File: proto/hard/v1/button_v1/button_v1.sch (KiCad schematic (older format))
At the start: 75 parts, among them J1 Conn_01x06_Female, J10 Conn_01x01_Female, J11 Conn_01x01_Female, J12 Conn_01x01_Female, J13 Conn_01x01_Female, J14 K3-2336D-combi, J15 Conn_01x03_Male, J16 Conn_01x01_Male, J2 Conn_01x06_Female, J3 Conn_01x06_Female, J4 Conn_01x06_Female, J7 Conn_01x04_Female, J9 Conn_01x01_Female, Q1 TP0610T, Q3 TP0610T, Q6 UMG8N, Q7 UMG8N, U1 LCD_2.8_SPI, U11 TC305, U12 OLED_0.96_I2C, U13 74HC595, U2 STM32F103C8Tx, U6 LM339, Y1 8MHz

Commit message: Schematic libs clean-up
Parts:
- U12: footprint MyModules:OLED_0.96_I2C -> brbuttonsystem:OLED_0.96_I2C; symbol MyModules:OLED_0.96_I2C -> brbuttonsystem:OLED_0.96_I2C
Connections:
- wire segments 191 -> 190
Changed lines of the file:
@@
 $Comp
 L brbuttonsystem:K3-2336D-combi J14
-U 1 1 5D188189
+U 2 1 5D188189
 P 7850 2850
 F 0 "J14" H 7950 2900 50  0000 C CNN
@@
 F 2 "brbuttonsystem:K3-2346D" H 7850 2850 50  0001 C CNN
 F 3 "" H 7850 2850 50  0001 C CNN
-	1    7850 2850
+	2    7850 2850
 	1    0    0    -1
 $EndComp
@@
 $EndComp
 Wire Wire Line
-	10250 1450 10250 1550
-Connection ~ 10250 1450
-Wire Wire Line
 	10250 1550 10100 1550
-Wire Wire Line
-	10250 1350 10250 1450
 Wire Wire Line
 	10100 1250 10250 1250
@@
 DISP_SCL
 $Comp
-L MyModules:OLED_0.96_I2C U12
+L brbuttonsystem:OLED_0.96_I2C U12
 U 1 1 5D23818B
 P 10350 950
 F 0 "U12" H 10350 1000 50  0000 L CNN
 F 1 "OLED_0.96_I2C" H 10350 300 50  0000 L CNN
-F 2 "MyModules:OLED_0.96_I2C" H 10350 950 50  0001 C CNN
+F 2 "brbuttonsystem:OLED_0.96_I2C" H 10350 950 50  0001 C CNN
 F 3 "" H 10350 950 50  0001 C CNN
 	1    10350 950
@@
 	-1   0    0    -1
 $EndComp
+Wire Wire Line
+	10250 1350 10250 1550
 $EndSCHEMATC

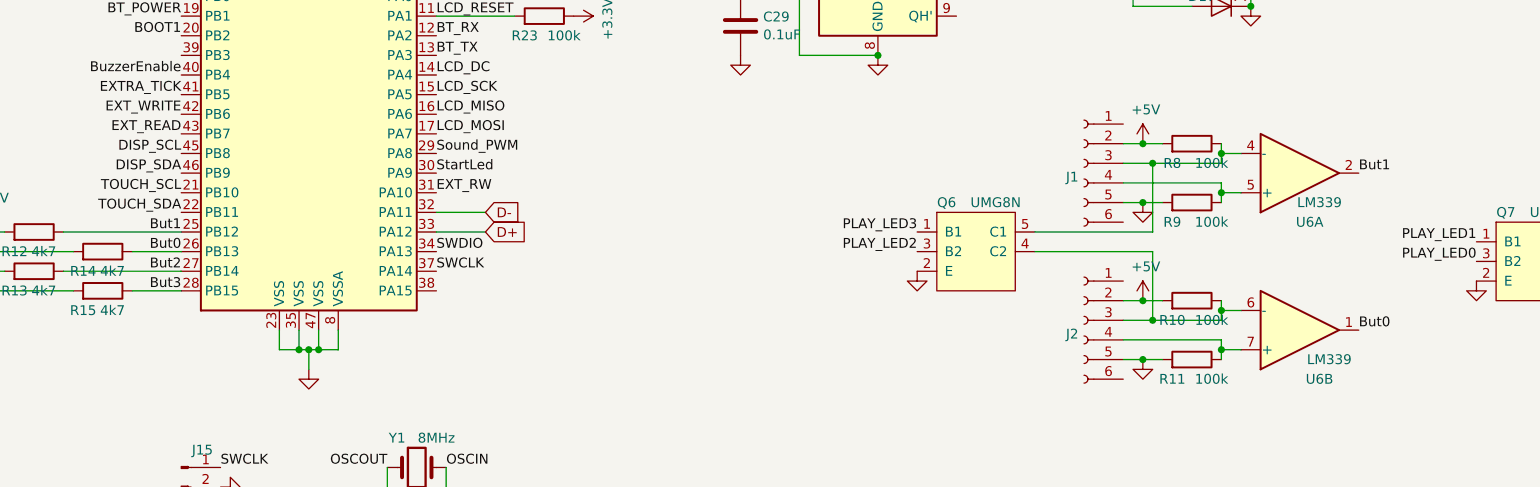
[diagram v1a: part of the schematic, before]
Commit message: Added example project with button connection schematic only. Corrected "dip" pins assignment to comply with main project.
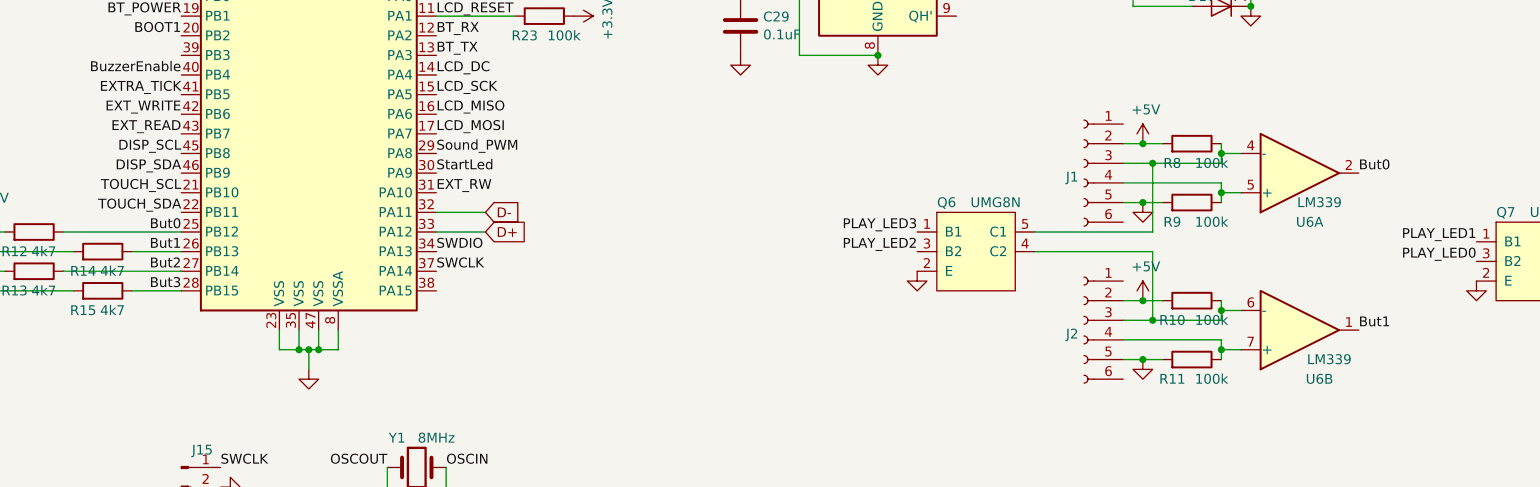
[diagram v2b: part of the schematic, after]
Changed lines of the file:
@@
 EESchema Schematic File Version 4
-LIBS:button_v1-cache
 EELAYER 29 0
 EELAYER END
@@
 $EndComp
 Connection ~ 10950 3900
+Text Label 7850 5000 0    50   ~ 0
+But0
 Text Label 7850 5800 0    50   ~ 0
-But0
-Text Label 7850 5000 0    50   ~ 0
 But1
 Text Label 10800 5000 0    50   ~ 0
@@
 Text Label 1850 5500 2    50   ~ 0
 But2
+Text Label 1850 5400 2    50   ~ 0
+But1
 Text Label 1850 5300 2    50   ~ 0
-But1
-Text Label 1850 5400 2    50   ~ 0
 But0
 Wire Wire Line

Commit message: Started schematic and PCB rework. Generated button_v1.pdf was left out of sync intentionally.
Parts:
- removed C28: 0.1uF, Capacitor_SMD:C_0805_2012Metric_Pad1.15x1.40mm_HandSolder, symbol Device:C
- removed D14, D15, D16, D17: LED, LED_THT:LED_D3.0mm_Clear, symbol Device:LED
- removed J14: K3-2336D-combi, brbuttonsystem:K3-2346D, symbol brbuttonsystem:K3-2336D-combi
- removed R12, R13, R14, R15, R41, R42: 4k7, Resistor_SMD:R_0805_2012Metric_Pad1.15x1.40mm_HandSolder, symbol Device:R
- removed U12: OLED_0.96_I2C, brbuttonsystem:OLED_0.96_I2C, symbol brbuttonsystem:OLED_0.96_I2C
- added J14: K3-2235D, brbuttonsystem:K3-2235D, symbol brbuttonsystem:K3-2235D
- added RN1: 4k7, Resistor_THT:R_Array_SIP5, symbol Device:R_Network04
- J7: footprint Connector_PinHeader_2.54mm:PinHeader_1x04_P2.54mm_Vertical -> Connector_PinHeader_2.54mm:PinHeader_1x04_P2.54mm_Horizontal
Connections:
- wire segments 190 -> 163
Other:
- moved on the sheet: D10, D11, D12, D13, R43, R44, R45, R46

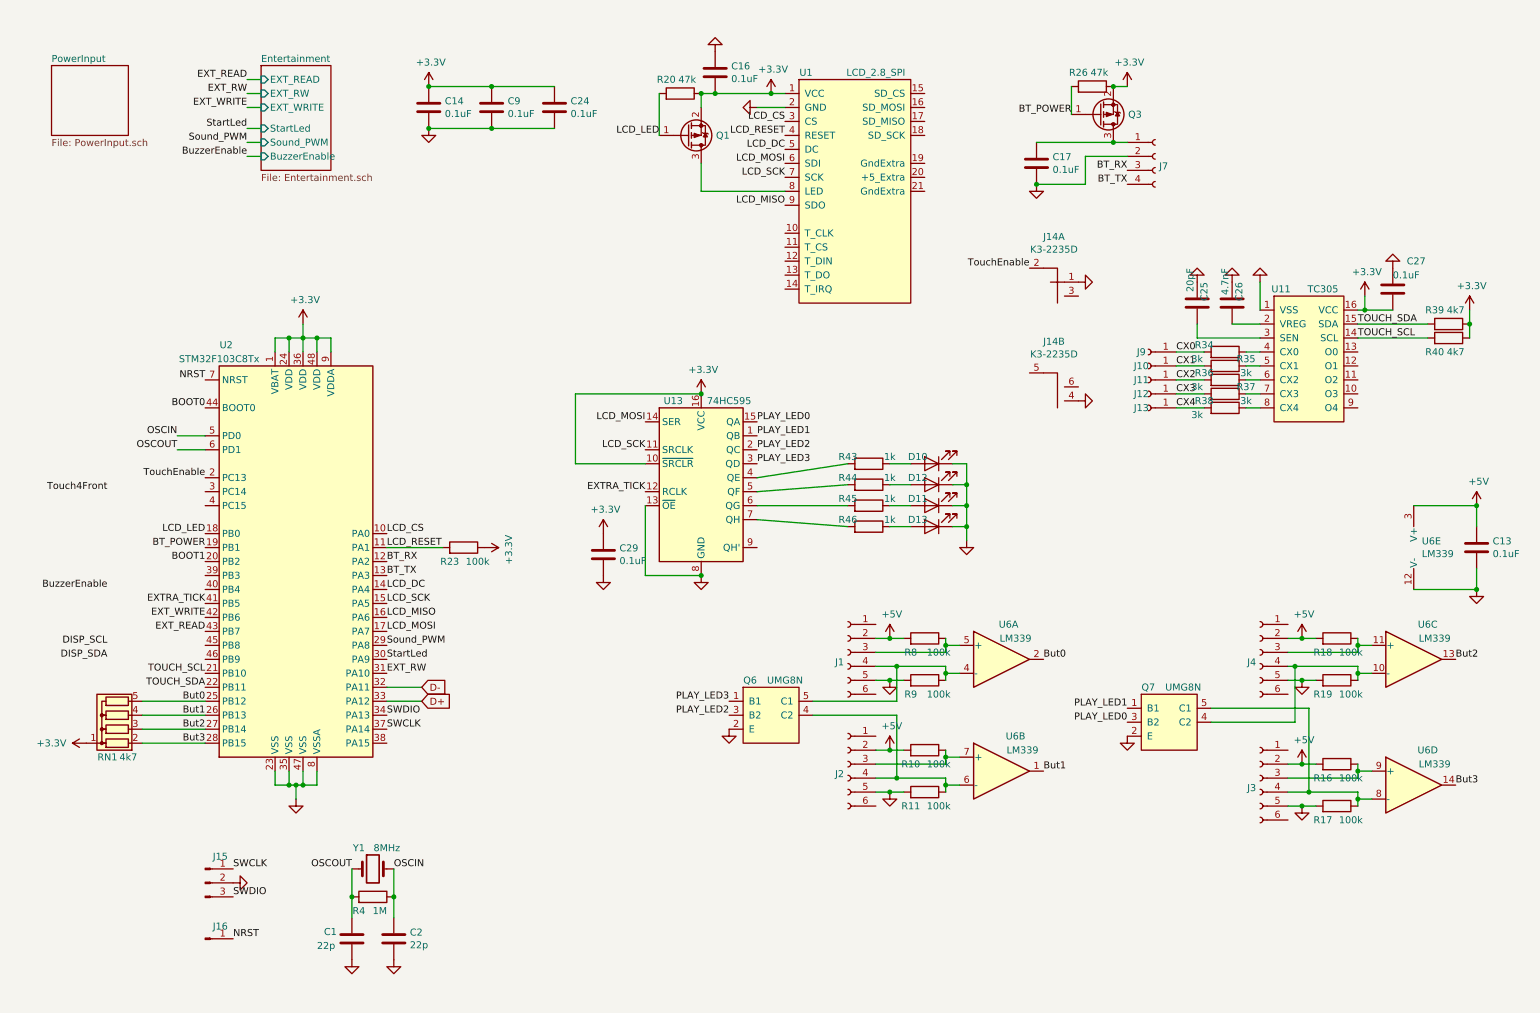
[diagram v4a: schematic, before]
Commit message: PCB rework in progress. Centered main LCD. Added second LCD. Button connectors we shifted to the right.
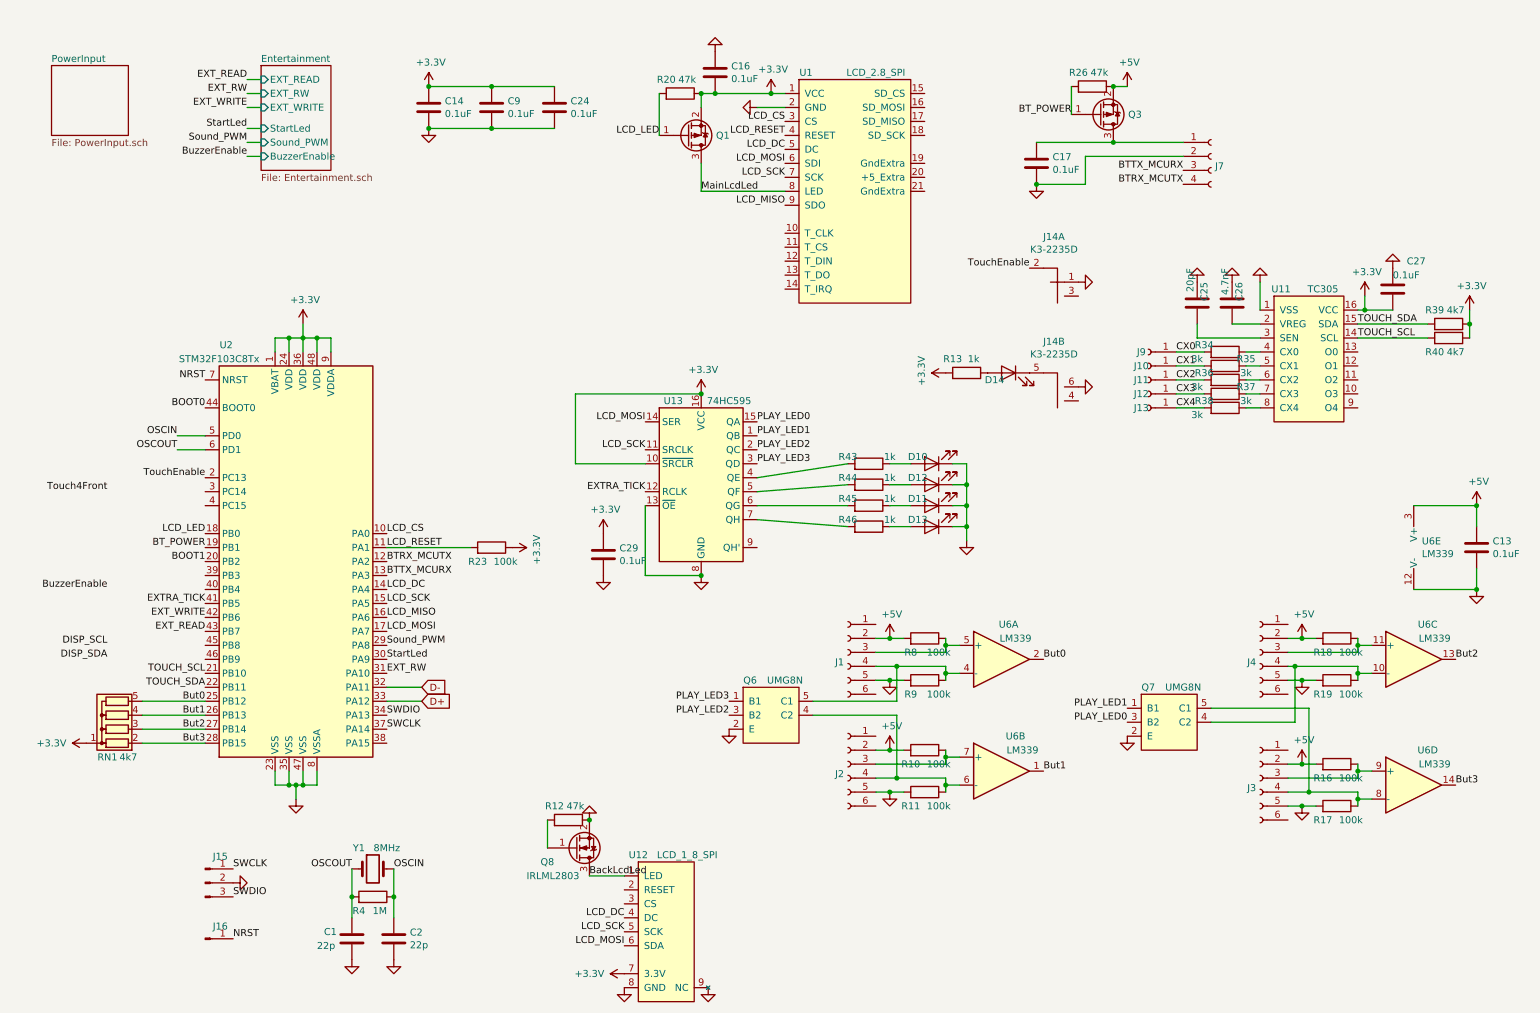
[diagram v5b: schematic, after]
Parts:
- added D14: LED, LED_THT:LED_D3.0mm_Clear, symbol Device:LED
- added Q8: IRLML2803, Package_TO_SOT_SMD:SOT-23, symbol Transistor_FET:IRLML2060
- added R12: 47k, Resistor_SMD:R_0805_2012Metric_Pad1.15x1.40mm_HandSolder, symbol Device:R
- added R13: 1k, Resistor_SMD:R_0805_2012Metric_Pad1.15x1.40mm_HandSolder, symbol Device:R
- added U12: LCD_1_8_SPI, brbuttonsystem:LCD_1_8_SPI, symbol brbuttonsystem:LCD_1_8_SPI
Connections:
- net +3V3: now also R13.2, U12.7 (3.3V); no longer Q3.2 (S), R26.1
- net +5V: now also Q3.2 (S), R26.1
- net GND: now also J14.6, Q8.2 (S), R12.1, U12.8 (GND), U12.9 (NC); no longer J14.4
- net LCD_DC: now also U12.4 (DC)
- net LCD_MOSI: now also U12.6 (SDA)
- net LCD_SCK: now also U12.5 (SCK)
- net MainLcdLed: now reaches Q1.3 (D), U1.8 (LED)
- net at J14.5: now also D14.1 (K)
- net BT_RX renamed BTRX_MCUTX
- net BTRX_MCUTX: now also J7.4 (Pin_4); no longer J7.3 (Pin_3)
- net BT_TX renamed BTTX_MCURX
- net BTTX_MCURX: now also J7.3 (Pin_3); no longer J7.4 (Pin_4)
- new net: Q8.1 (G), R12.2
- new net: D14.2 (A), R13.1
- new net BackLcdLed: Q8.3 (D), U12.1 (LED)
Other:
- moved on the sheet: J7, R23
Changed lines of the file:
@@
 	1    0    0    1
-$EndComp
-$Comp
-L Device:R R20
-U 1 1 5D14F380
-P 5250 950
-F 0 "R20" V 5350 850 50  0000 C CNN
-F 1 "47k" V 5350 1000 50  0000 C CNN
-F 2 "Resistor_SMD:R_0805_2012Metric_Pad1.15x1.40mm_HandSolder" V 5180 950 50  0001 C CNN
-F 3 "~" H 5250 950 50  0001 C CNN
-	1    5250 950
-	0    1    -1   0
 $EndComp
 Wire Wire Line
@@
 $EndComp
 Wire Wire Line
-	3550 4200 3150 4200
+	3750 4200 3150 4200
 Text Label 1850 5100 2    50   ~ 0
 TOUCH_SCL
@@
 BT_POWER
 Text Label 3150 4400 0    50   ~ 0
-BT_TX
+BTTX_MCURX
 Text Label 3150 4300 0    50   ~ 0
-BT_RX
+BTRX_MCUTX
 Text Label 3150 5000 0    50   ~ 0
 StartLed
@@
 L power:+3.3V #PWR044
 U 1 1 5D2A8270
-P 3850 4200
-F 0 "#PWR044" H 3850 4050 50  0001 C CNN
-F 1 "+3.3V" H 3865 4373 50  0000 C CNN
-F 2 "" H 3850 4200 50  0001 C CNN
-F 3 "" H 3850 4200 50  0001 C CNN
-	1    3850 4200
+P 4050 4200
+F 0 "#PWR044" H 4050 4050 50  0001 C CNN
+F 1 "+3.3V" H 4065 4373 50  0000 C CNN
+F 2 "" H 4050 4200 50  0001 C CNN
+F 3 "" H 4050 4200 50  0001 C CNN
+	1    4050 4200
 	0    1    1    0
 $EndComp
@@
 L Device:R R23
 U 1 1 5D2A77C8
-P 3700 4200
-F 0 "R23" V 3600 4100 50  0000 C CNN
-F 1 "100k" V 3600 4300 50  0000 C CNN
-F 2 "Resistor_SMD:R_0805_2012Metric_Pad1.15x1.40mm_HandSolder" V 3630 4200 50  0001 C CNN
-F 3 "~" H 3700 4200 50  0001 C CNN
-	1    3700 4200
+P 3900 4200
+F 0 "R23" V 3800 4100 50  0000 C CNN
+F 1 "100k" V 3800 4300 50  0000 C CNN
+F 2 "Resistor_SMD:R_0805_2012Metric_Pad1.15x1.40mm_HandSolder" V 3830 4200 50  0001 C CNN
+F 3 "~" H 3900 4200 50  0001 C CNN
+	1    3900 4200
 	0    1    -1   0
 $EndComp
@@
 L Connector:Conn_01x04_Female J7
 U 1 1 5D0CCB3B
-P 8650 1400
-F 0 "J7" H 8678 1330 50  0000 L CNN
-F 1 "Conn_01x04_Female" H 8678 1285 50  0001 L CNN
-F 2 "Connector_PinHeader_2.54mm:PinHeader_1x04_P2.54mm_Horizontal" H 8650 1400 50  0001 C CNN
-F 3 "~" H 8650 1400 50  0001 C CNN
-	1    8650 1400
+P 9050 1400
+F 0 "J7" H 9078 1330 50  0000 L CNN
+F 1 "Conn_01x04_Female" H 9078 1285 50  0001 L CNN
+F 2 "Connector_PinHeader_2.54mm:PinHeader_1x04_P2.54mm_Horizontal" H 9050 1400 50  0001 C CNN
+F 3 "~" H 9050 1400 50  0001 C CNN
+	1    9050 1400
 	1    0    0    -1
 $EndComp
@@
 	8350 1300 7800 1300
 Connection ~ 8350 1300
-$Comp
-L power:+3.3V #PWR049
-U 1 1 5D108701
-P 8450 900
-F 0 "#PWR049" H 8450 750 50  0001 C CNN
-F 1 "+3.3V" H 8465 1073 50  0000 C CNN
-F 2 "" H 8450 900 50  0001 C CNN
-F 3 "" H 8450 900 50  0001 C CNN
-	1    8450 900
-	1    0    0    -1
-$EndComp
 Connection ~ 7800 1600
 Wire Wire Line
@@
 	8150 1400 8150 1600
 Wire Wire Line
-	8450 1400 8150 1400
-Wire Wire Line
-	8450 1300 8350 1300
+	8850 1400 8150 1400
+Wire Wire Line
+	8850 1300 8350 1300
 $Comp
 L Device:C C17
@@
 	1    0    0    -1
 $EndComp
-Text Label 8450 1500 2    50   ~ 0
-BT_RX
-Text Label 8450 1600 2    50   ~ 0
-BT_TX
 $Comp
 L power:GND #PWR0120
 U 1 1 5D194DEC
-P 8100 3150
-F 0 "#PWR0120" H 8100 2900 50  0001 C CNN
-F 1 "GND" H 8105 2977 50  0001 C CNN
-F 2 "" H 8100 3150 50  0001 C CNN
-F 3 "" H 8100 3150 50  0001 C CNN
-	1    8100 3150
+P 8100 3050
+F 0 "#PWR0120" H 8100 2800 50  0001 C CNN
+F 1 "GND" H 8105 2877 50  0001 C CNN
+F 2 "" H 8100 3050 50  0001 C CNN
+F 3 "" H 8100 3050 50  0001 C CNN
+	1    8100 3050
 	0    -1   -1   0
 $EndComp
@@
 Wire Wire Line
 	1400 5300 1850 5300
+$Comp
+L brbuttonsystem:LCD_1_8_SPI U12
+U 1 1 5D664791
+P 4950 6450
+F 0 "U12" H 4950 6500 50  0000 C CNN
+F 1 "LCD_1_8_SPI" H 5300 6500 50  0000 C CNN
+F 2 "brbuttonsystem:LCD_1_8_SPI" H 4950 6450 50  0001 C CNN
+F 3 "" H 4950 6450 50  0001 C CNN
+	1    4950 6450
+	1    0    0    -1
+$EndComp
+$Comp
+L power:GND #PWR0121
+U 1 1 5D66C20A
+P 4850 7350
+F 0 "#PWR0121" H 4850 7100 50  0001 C CNN
+F 1 "GND" H 4855 7177 50  0001 C CNN
+F 2 "" H 4850 7350 50  0001 C CNN
+F 3 "" H 4850 7350 50  0001 C CNN
+	1    4850 7350
+	1    0    0    -1
+$EndComp
+$Comp
+L power:+3.3V #PWR0122
+U 1 1 5D66EC1A
+P 4850 7250
+F 0 "#PWR0122" H 4850 7100 50  0001 C CNN
+F 1 "+3.3V" V 4850 7500 50  0000 C CNN
+F 2 "" H 4850 7250 50  0001 C CNN
+F 3 "" H 4850 7250 50  0001 C CNN
+	1    4850 7250
+	0    -1   -1   0
+$EndComp
+$Comp
+L power:GND #PWR0141
+U 1 1 5D68AB1C
+P 5450 7350
+F 0 "#PWR0141" H 5450 7100 50  0001 C CNN
+F 1 "GND" H 5455 7177 50  0001 C CNN
+F 2 "" H 5450 7350 50  0001 C CNN
+F 3 "" H 5450 7350 50  0001 C CNN
+	1    5450 7350
+	1    0    0    -1
+$EndComp
+Text Label 4850 6950 2    50   ~ 0
+LCD_SCK
+Text Label 4850 7050 2    50   ~ 0
+LCD_MOSI
+Text Label 4850 6850 2    50   ~ 0
+LCD_DC
+$Comp
+L Transistor_FET:IRLML2060 Q8
+U 1 1 5D68AB43
+P 4500 6350
+F 0 "Q8" H 4250 6450 50  0000 L CNN
+F 1 "IRLML2803" H 4150 6550 50  0000 L CNN
+F 2 "Package_TO_SOT_SMD:SOT-23" H 4700 6275 50  0001 L CIN
+F 3 "https://www.infineon.com/dgdl/irlml2060pbf.pdf?fileId=5546d462533600a401535664b7fb25ee" H 4500 6350 50  0001 L CNN
+	1    4500 6350
+	1    0    0    1
+$EndComp
+Wire Wire Line
+	4850 6550 4600 6550
+$Comp
+L Device:R R20
+U 1 1 5D14F380
+P 5250 950
+F 0 "R20" V 5350 850 50  0000 C CNN
+F 1 "47k" V 5350 1000 50  0000 C CNN
+F 2 "Resistor_SMD:R_0805_2012Metric_Pad1.15x1.40mm_HandSolder" V 5180 950 50  0001 C CNN
+F 3 "~" H 5250 950 50  0001 C CNN
+	1    5250 950
+	0    1    -1   0
+$EndComp
+$Comp
+L Device:R R12
+U 1 1 5D6CBE16
+P 4450 6150
+F 0 "R12" V 4550 6050 50  0000 C CNN
+F 1 "47k" V 4550 6200 50  0000 C CNN
+F 2 "Resistor_SMD:R_0805_2012Metric_Pad1.15x1.40mm_HandSolder" V 4380 6150 50  0001 C CNN
+F 3 "~" H 4450 6150 50  0001 C CNN
+	1    4450 6150
+	0    1    -1   0
+$EndComp
+Wire Wire Line
+	4300 6350 4300 6150
+$Comp
+L power:GND #PWR0142
+U 1 1 5D6EB51B
+P 4600 6150
+F 0 "#PWR0142" H 4600 5900 50  0001 C CNN
+F 1 "GND" H 4605 5977 50  0001 C CNN
+F 2 "" H 4600 6150 50  0001 C CNN
+F 3 "" H 4600 6150 50  0001 C CNN
+	1    4600 6150
+	-1   0    0    1
+$EndComp
+Connection ~ 4600 6150
+Text Label 5400 1650 0    50   ~ 0
+MainLcdLed
+Text Label 4600 6550 0    50   ~ 0
+BackLcdLed
+Text Label 8850 1600 2    50   ~ 0
+BTRX_MCUTX
+Text Label 8850 1500 2    50   ~ 0
+BTTX_MCURX
+$Comp
+L power:+5V #PWR0143
+U 1 1 5D7D21F9
+P 8450 900
+F 0 "#PWR0143" H 8450 750 50  0001 C CNN
+F 1 "+5V" H 8465 1073 50  0000 C CNN
+F 2 "" H 8450 900 50  0001 C CNN
+F 3 "" H 8450 900 50  0001 C CNN
+	1    8450 900
+	1    0    0    -1
+$EndComp
+$Comp
+L Device:LED D14
+U 1 1 5D80F7D1
+P 7600 2950
+F 0 "D14" H 7700 2900 50  0000 C CNN
+F 1 "LED" H 7593 2786 50  0001 C CNN
+F 2 "LED_THT:LED_D3.0mm_Clear" H 7600 2950 50  0001 C CNN
+F 3 "~" H 7600 2950 50  0001 C CNN
+	1    7600 2950
+	-1   0    0    -1
+$EndComp
+$Comp
+L Device:R R13
+U 1 1 5D811781
+P 7300 2950
+F 0 "R13" V 7400 2850 50  0000 C CNN
+F 1 "1k" V 7400 3000 50  0000 C CNN
+F 2 "Resistor_SMD:R_0805_2012Metric_Pad1.15x1.40mm_HandSolder" V 7230 2950 50  0001 C CNN
+F 3 "~" H 7300 2950 50  0001 C CNN
+	1    7300 2950
+	0    1    -1   0
+$EndComp
+$Comp
+L power:+3.3V #PWR0144
+U 1 1 5D813CB3
+P 7150 2950
+F 0 "#PWR0144" H 7150 2800 50  0001 C CNN
+F 1 "+3.3V" H 7165 3123 50  0000 C CNN
+F 2 "" H 7150 2950 50  0001 C CNN
+F 3 "" H 7150 2950 50  0001 C CNN
+	1    7150 2950
+	0    -1   -1   0
+$EndComp
 $EndSCHEMATC
